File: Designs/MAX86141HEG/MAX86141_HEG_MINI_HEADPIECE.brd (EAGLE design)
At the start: 249.4 x 28.6 mm, 6 parts

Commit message: updates,
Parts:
- moved D1 6.53 mm to (255.9, 61.4)
- moved D2 6.53 mm to (255.9, 58.4)
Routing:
- net LED2: track 208.7 -> 215.2 mm
- net LED1: track 207.8 -> 214.4 mm
- net GND: track 332.4 -> 338.9 mm
- net MISO: track 158.2 -> 158.8 mm
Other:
- board size 249.4 x 28.6 mm -> 256 x 28.6 mm

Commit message: updates/another fix for boot routine
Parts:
- moved D1 9.31 mm to (252.3, 52.8)
- moved D2 9.31 mm to (252.3, 49.8)
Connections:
- net GPIO1: now also JP4.6
- net GPIO2: now also JP4.5
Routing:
- net GPIO2: track 0.00 -> 176.5 mm, vias 0 -> 2
- net GPIO1: track 0.00 -> 170.5 mm, vias 0 -> 2
- net GND: track 338.9 -> 349.2 mm
- net LED2: track 215.2 -> 220.2 mm, vias 2 -> 3
- net LED1: track 214.4 -> 210.7 mm, vias 2 -> 3
- net 3.3V: track 171.2 -> 174.5 mm, vias 2 -> 4
- net MOSI: track 158.9 -> 161.4 mm, vias 0 -> 2
- net MISO: track 158.8 -> 161.2 mm, vias 0 -> 2
- net SS: track 160.2 -> 162.4 mm, vias 0 -> 2
- net PD_GND: track 172.9 -> 171.3 mm
- net SCLK: track 170.5 -> 171.9 mm, vias 3 -> 4
- net INT: track 165.5 -> 166.6 mm, vias 3 -> 4
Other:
- board size 256 x 28.6 mm -> 252.5 x 28.6 mm

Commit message: quality improvements to design (hopefully)
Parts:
- added R1, R2: (no value), adafruit:0204/5
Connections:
- new net VLED1: JP4.16, R2.2
- new net VLED2: JP4.15, R1.2
- net LED1: now also R2.1; no longer JP4.16
- net LED2: now also R1.1; no longer JP4.15
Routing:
- net VLED2: track 0.00 -> 12.0 mm
- net 3.3V: track 174.5 -> 183.0 mm
- net LED2: track 220.2 -> 212.0 mm, vias 3 -> 1
- net LED1: track 210.7 -> 203.1 mm, vias 3 -> 1
- net VLED1: track 0.00 -> 6.75 mm
- net MISO: track 161.2 -> 166.9 mm
- net MOSI: track 161.4 -> 166.9 mm
- net INT: track 166.6 -> 171.6 mm
- net SCLK: track 171.9 -> 176.7 mm
- net SS: track 162.4 -> 166.6 mm
- net PD_GND: track 171.3 -> 172.0 mm

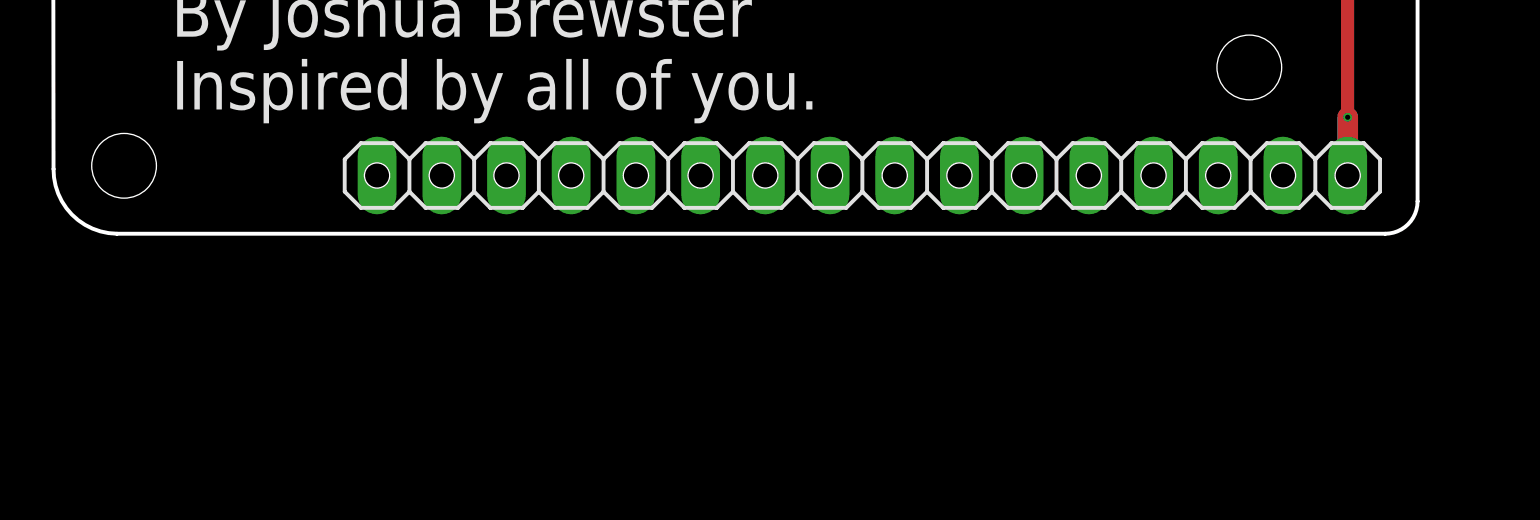
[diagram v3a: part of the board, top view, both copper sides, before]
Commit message: headpiece update with switches
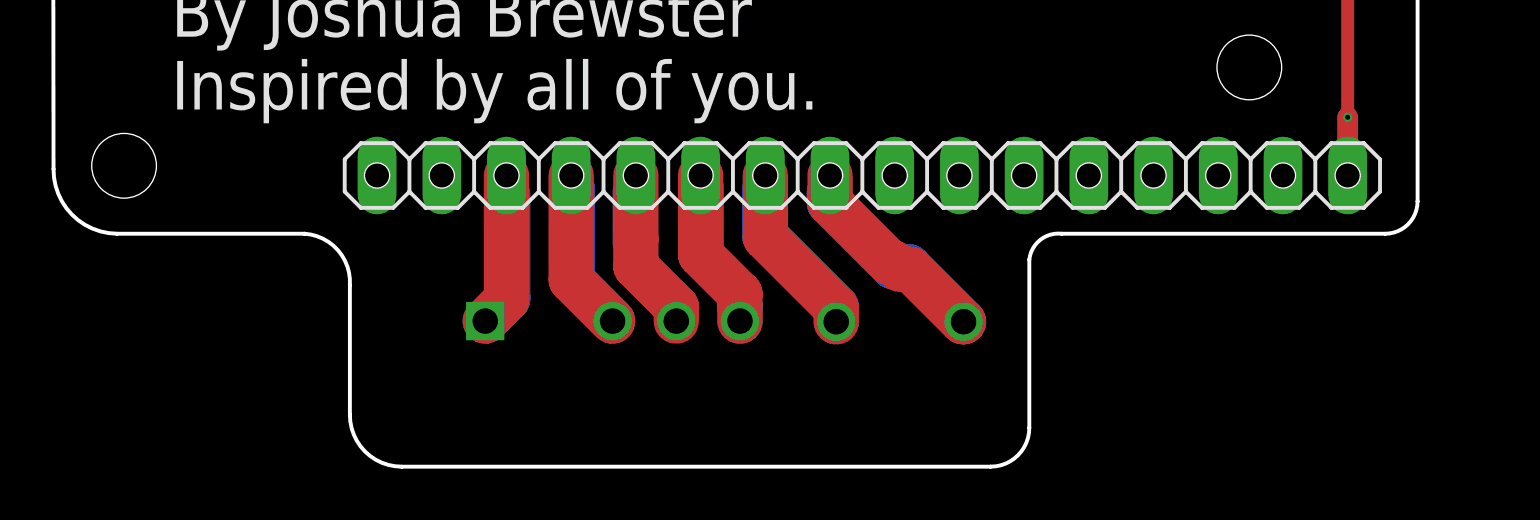
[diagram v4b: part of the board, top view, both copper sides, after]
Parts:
- added S1: BUTT-2, BUTT-2:SW_BUTT-2
- added U1: OS103012MU2QP1, OS103012MU2QP1:SW_OS103012MU2QP1
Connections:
- new net N$1: JP1.3, U1.1
- new net N$2: JP1.4, U1.2
- new net N$3: JP1.5, U1.3
- new net N$4: JP1.6, U1.4
- new net N$5: JP1.7, S1.2
- new net N$6: JP1.8, S1.1
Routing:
- net N$6: track 0.00 -> 15.9 mm
- net N$3: track 0.00 -> 15.0 mm
- net N$5: track 0.00 -> 13.2 mm
- net N$2: track 0.00 -> 12.2 mm
- net N$4: track 0.00 -> 12.2 mm
- net N$1: track 0.00 -> 11.4 mm
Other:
- board size 252.5 x 28.6 mm -> 252.5 x 37.7 mm
- board text added: "BLE WIFI BT"
- board text added: "SLEEP"

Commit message: fix
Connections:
- removed net N$6: JP1.8, S1.1
- net 3.3V: now also S1.1
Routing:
- net 3.3V: track 183.0 -> 208.6 mm, vias 4 -> 5
- net N$6: track 15.9 -> 0.00 mm
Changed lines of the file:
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@@
 <attribute name="MF" value="Gravitech" x="44.196" y="33.3756" size="1.778" layer="28" rot="MR0" display="off"/>
 <attribute name="MP" value="BUTT-2" x="44.196" y="33.3756" size="1.778" layer="28" rot="MR0" display="off"/>
-<attribute name="NAME" x="45.2148" y="34.7166" size="1.27" layer="26" rot="MR0"/>
+<attribute name="NAME" x="44.1734" y="34.7674" size="1.27" layer="26" rot="MR0"/>
 <attribute name="PACKAGE" value="None" x="44.196" y="33.3756" size="1.778" layer="28" rot="MR0" display="off"/>
 <attribute name="PRICE" value="None" x="44.196" y="33.3756" size="1.778" layer="28" rot="MR0" display="off"/>
@@
 <via x="197.4342" y="58.0644" extent="1-16" drill="0.2"/>
 <wire x1="197.4342" y1="58.0644" x2="198.628" y2="56.8706" width="0.4064" layer="16"/>
+<contactref element="S1" pad="1"/>
+<wire x1="46.696" y1="33.3756" x2="47.204" y2="33.8836" width="1.778" layer="16"/>
+<wire x1="47.204" y1="33.8836" x2="47.2294" y2="33.8836" width="1.778" layer="16"/>
+<wire x1="46.696" y1="33.3756" x2="47.204" y2="33.8836" width="1.778" layer="1"/>
+<wire x1="47.204" y1="33.8836" x2="47.2294" y2="33.8582" width="1.778" layer="1"/>
+<wire x1="47.8028" y1="34.4824" x2="46.696" y2="33.3756" width="0.3048" layer="1"/>
+<wire x1="47.8028" y1="35.687" x2="47.8028" y2="34.4824" width="0.3048" layer="1"/>
+<wire x1="47.2294" y1="33.8836" x2="47.8028" y2="34.457" width="0.3048" layer="16"/>
+<wire x1="47.8028" y1="34.457" x2="47.8028" y2="35.687" width="0.3048" layer="16"/>
+<via x="47.8028" y="35.687" extent="1-16" drill="0.35"/>
+<wire x1="47.8028" y1="35.687" x2="47.8028" y2="40.8178" width="0.3048" layer="16"/>
+<wire x1="47.8028" y1="40.8178" x2="48.3362" y2="41.3512" width="0.3048" layer="16"/>
+<wire x1="61.722" y1="41.3512" x2="61.7728" y2="41.402" width="0.3048" layer="16"/>
+<wire x1="61.722" y1="41.3512" x2="48.3362" y2="41.3512" width="0.3048" layer="16"/>
 </signal>
 <signal name="GPIO1">
@@
 <wire x1="38.9128" y1="36.6922" x2="38.9128" y2="39.116" width="1.778" layer="1"/>
 </signal>
-<signal name="N$6">
-<contactref element="JP1" pad="8"/>
-<contactref element="S1" pad="1"/>
-<wire x1="44.196" y1="35.433" x2="43.942" y2="35.687" width="0.4064" layer="1"/>
-<wire x1="46.696" y1="33.3756" x2="44.537" y2="35.5346" width="1.778" layer="16"/>
-<wire x1="44.537" y1="35.5346" x2="43.942" y2="35.5346" width="1.778" layer="16"/>
-<wire x1="43.942" y1="35.5346" x2="41.4274" y2="38.0492" width="1.778" layer="16"/>
-<wire x1="41.4274" y1="38.0492" x2="41.4274" y2="38.481" width="1.778" layer="16"/>
-<wire x1="41.4528" y1="38.0492" x2="41.4528" y2="39.116" width="1.778" layer="1"/>
-<wire x1="44.6132" y1="35.433" x2="44.196" y2="35.433" width="1.778" layer="1"/>
-<wire x1="46.696" y1="33.3756" x2="46.6706" y2="33.3756" width="1.778" layer="1"/>
-<wire x1="46.6706" y1="33.3756" x2="44.6132" y2="35.433" width="1.778" layer="1"/>
-<wire x1="43.942" y1="35.687" x2="43.815" y2="35.687" width="1.778" layer="1"/>
-<wire x1="43.815" y1="35.687" x2="41.4528" y2="38.0492" width="1.778" layer="1"/>
-</signal>
 </signals>

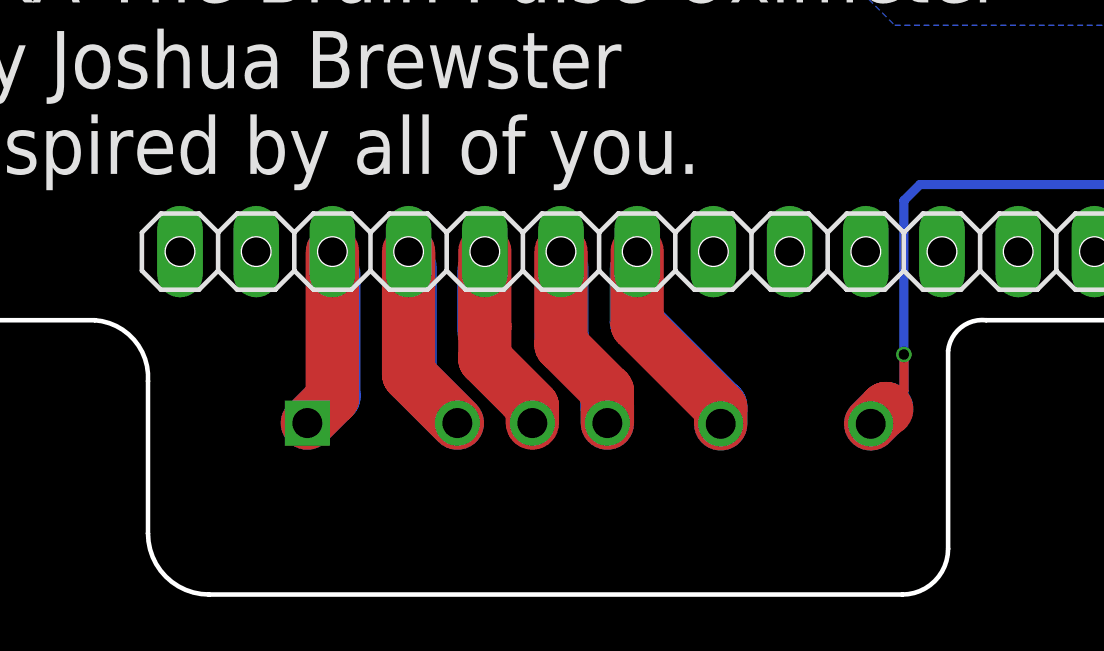
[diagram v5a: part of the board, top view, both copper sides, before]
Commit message: more holes for switch mount
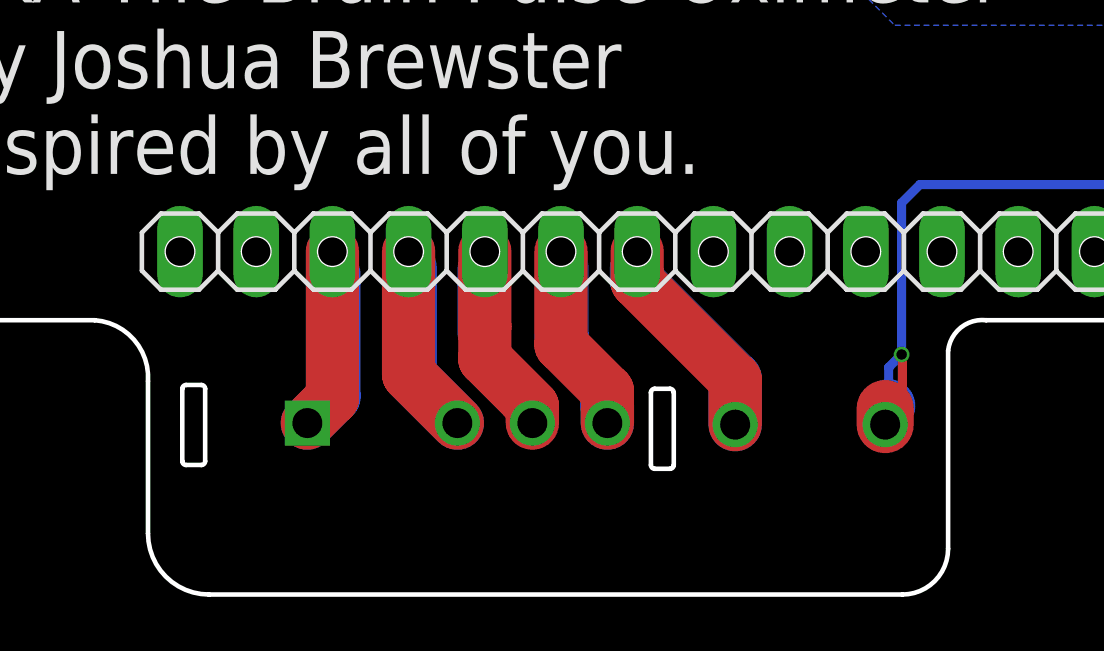
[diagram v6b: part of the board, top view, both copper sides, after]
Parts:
- moved S1 0.48 mm to (44.7, 33.4)
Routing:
- net 3.3V: track 208.6 -> 207.5 mm
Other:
- outline, holes or cut-outs redrawn
